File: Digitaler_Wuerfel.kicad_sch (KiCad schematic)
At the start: 40 parts, among them J1 Conn_01x03_Pin, J2 Conn_02x03_Odd_Even, SW1 SW_Push, SW2 SW_Push, SW3 SW_Push, SW4 SW_SPST, U1 74HC595, U2 74HC595, U3 ATmega328PB-A, U4 LM7805_TO220

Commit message: Started tracing
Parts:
- removed C3, C6: C_Polarized, symbol Device:C_Polarized
- removed D1: D_Zener, symbol Device:D_Zener
- removed U4: LM7805_TO220, Package_TO_SOT_THT:TO-220-3_Horizontal_TabDown, symbol Regulator_Linear:LM7805_TO220
- added C1, C7: 470pF, Capacitor_SMD:C_0805_2012Metric_Pad1.18x1.45mm_HandSolder, symbol Device:C
- added C2: 0.1uF, Capacitor_SMD:C_0805_2012Metric_Pad1.18x1.45mm_HandSolder, symbol Device:C
- added C8: 2.2uF, Capacitor_Tantalum_SMD:CP_EIA-3528-21_Kemet-B_Pad1.50x2.35mm_HandSolder, symbol Device:C_Polarized
- added Q1: 2N3904, Package_TO_SOT_THT:TO-92_Inline, symbol Transistor_BJT:2N3904
- added R1: 200k, Resistor_SMD:R_0805_2012Metric_Pad1.20x1.40mm_HandSolder, symbol Device:R
- added R11, R12: 1k, Resistor_SMD:R_0805_2012Metric_Pad1.20x1.40mm_HandSolder, symbol Device:R
- added TP1, TP2, TP3, TP4, TP5, TP6: TestPoint_Probe, TestPoint:TestPoint_Pad_D2.0mm, symbol Connector:TestPoint_Probe
- added U1, U2: MAX2650EUS+T, MAX2650EUS+T:21-0052F_MXM, symbol MAX2650EUS+T:MAX2650EUS+T
- added U5: MIC5219-5.0YM5, Package_TO_SOT_SMD:SOT-23-5, symbol Regulator_Linear:MIC5219-5.0YM5
- C5: value C -> 470pF
- C6: renamed from C4; value C -> 1uF
- D1: renamed from D2; footprint (none) -> Diode_SMD:D_SOD-323_HandSoldering
- R2: renamed from R1; value R -> 10k
- R3: renamed from R2; value R -> 10k
- R4: renamed from R3; value R -> 10k
- SW1, SW2: footprint (none) -> Button_Switch_THT:SW_PUSH-12mm_Wuerth-430476085716
- SW3: footprint (none) -> Button_Switch_THT:SW_PUSH_6mm_H5mm
- SW4: footprint (none) -> Button_Switch_THT:SW_E-Switch_EG1271_SPDT
- renumbered C1 to C3, C2 to C4, J2 to J1, J1 to J2, R9 to R10, R10 to R13, R11 to R14, R12 to R15, R13 to R16, R14 to R17, R15 to R18, R16 to R19, R17 to R20, R18 to R21, R19 to R22, R4 to R5, R5 to R6, R6 to R7, R7 to R8, R8 to R9, U1 to U3, U2 to U4, U3 to U6
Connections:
- net +5V: now also C2.2, C8.1, R11.1, TP5.1, U1.4 (VCC), U2.4 (VCC), U5.5 (OUT); no longer C5.1
- net +9V: now also R1.1; no longer U6.28 (PC5)
- net GND: now also C2.1, C7.2, C8.2, Q1.2 (B), R12.2, TP6.1, U1.2 (GND), U2.2 (GND), U5.2 (GND); no longer C5.2
- net at C6.1, D1.1 (K): now also U5.1 (IN), U5.3 (EN)
- new net: C1.2, U1.1 (IN)
- new net: TP2.1, U1.3 (OUT), U2.1 (IN)
- new net: C1.1, Q1.1 (E), R1.2, TP1.1
- new net: C7.1, U5.4 (BP)
- new net: C5.1, TP3.1, U2.3 (OUT)
- new net ENTROPY: C5.2, R11.2, R12.1, TP4.1, U6.28 (PC5)
- no-connect marks 17 -> 18
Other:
- note added: "White Noise Generator"
- moved on the sheet: AFF1, AFF2, BT1, C3, C4, C6, D1, J1, J2, R10, R13, R14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

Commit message: Finished tracing
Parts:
- removed TP3: TestPoint_Probe, TestPoint:TestPoint_Pad_D2.0mm, symbol Connector:TestPoint_Probe
- removed U2: MAX2650EUS+T, MAX2650EUS+T:21-0052F_MXM, symbol MAX2650EUS+T:MAX2650EUS+T
- added JP1: SolderJumper_2_Open, Jumper:SolderJumper-2_P1.3mm_Open_TrianglePad1.0x1.5mm, symbol Jumper:SolderJumper_2_Open
- renumbered R8 to R10, R9 to R11, R10 to R12, R11 to R5, R12 to R6, R5 to R7, R6 to R8, R7 to R9, TP4 to TP3, TP5 to TP4, TP6 to TP5, U3 to U2, U4 to U3, U5 to U4, U6 to U5
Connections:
- net +9V: now also C6.1, D1.1 (K), U4.1 (IN), U4.3 (EN); no longer BT1.1 (+), SW4.1 (A)
- net ENTROPY: now also JP1.2 (B); no longer C5.2, R5.2, R6.1, TP3.1
- net at TP2.1, U1.3 (OUT): now also C5.1
- new net: C5.2, JP1.1 (A), R5.2, R6.1, TP3.1
- new net: BT1.1 (+), SW4.1 (A)
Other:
- moved on the sheet: C1, C2, C5, Q1, R1, R5, R6, TP1, TP2, TP3, U1

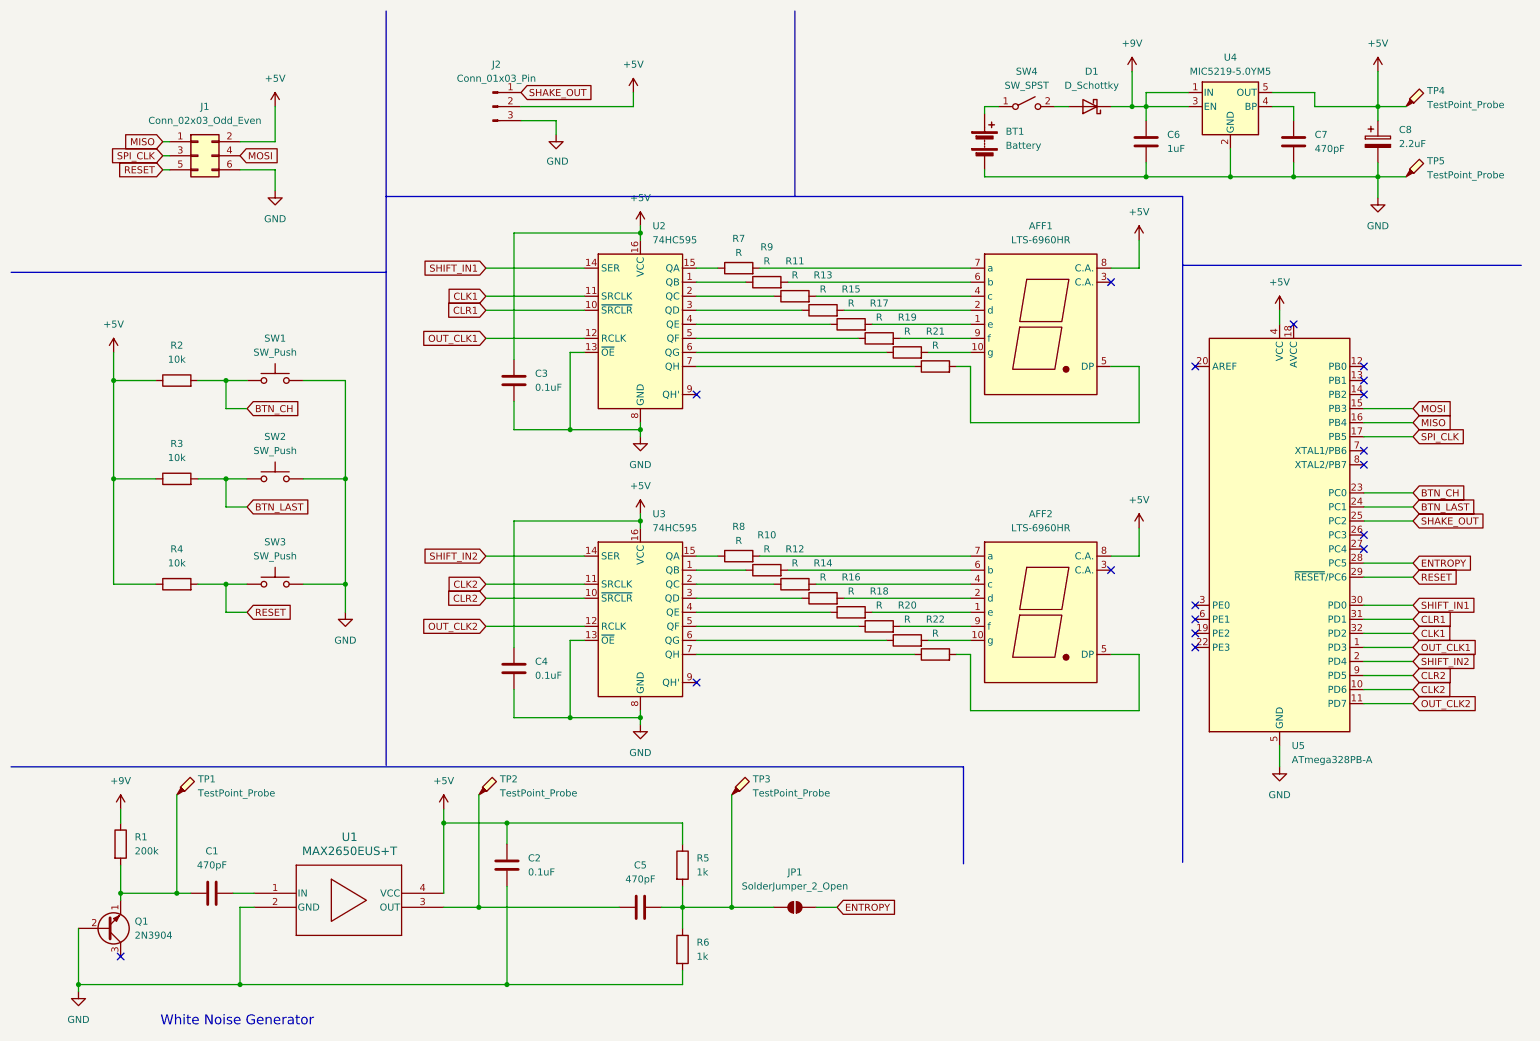
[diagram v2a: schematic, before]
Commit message: Added decoupling capacitors and ground plane
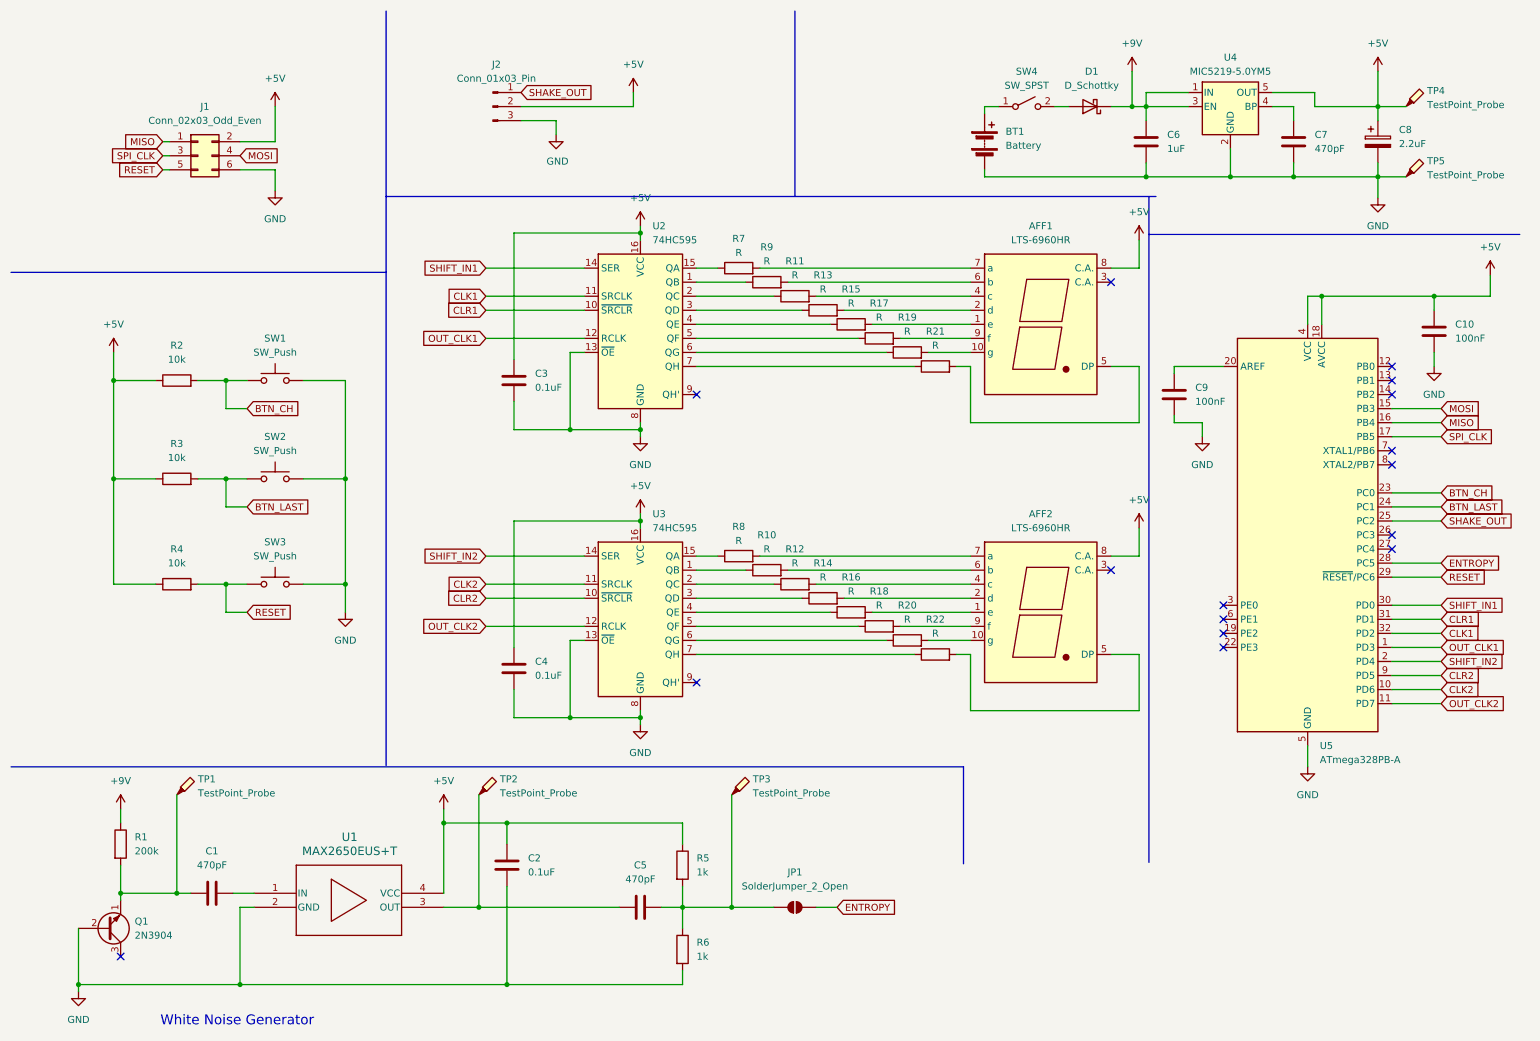
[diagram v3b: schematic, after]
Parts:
- added C10, C9: 100nF, Capacitor_SMD:C_0805_2012Metric_Pad1.18x1.45mm_HandSolder, symbol Device:C
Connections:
- net +5V: now also U5.18 (AVCC), C10.1
- net GND: now also C10.2, C9.2
- net at U5.20 (AREF): now also C9.1
- no-connect marks 18 -> 16
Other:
- moved on the sheet: U5
